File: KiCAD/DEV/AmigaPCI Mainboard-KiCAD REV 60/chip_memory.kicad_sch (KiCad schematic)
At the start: 25 parts, among them U701 74LVC245, U702 74LVC245, U703 74LVC245, U704 74LVC245, U705 74LVC245, U706 74LVC245, U707 SDRAM(8Mx32)

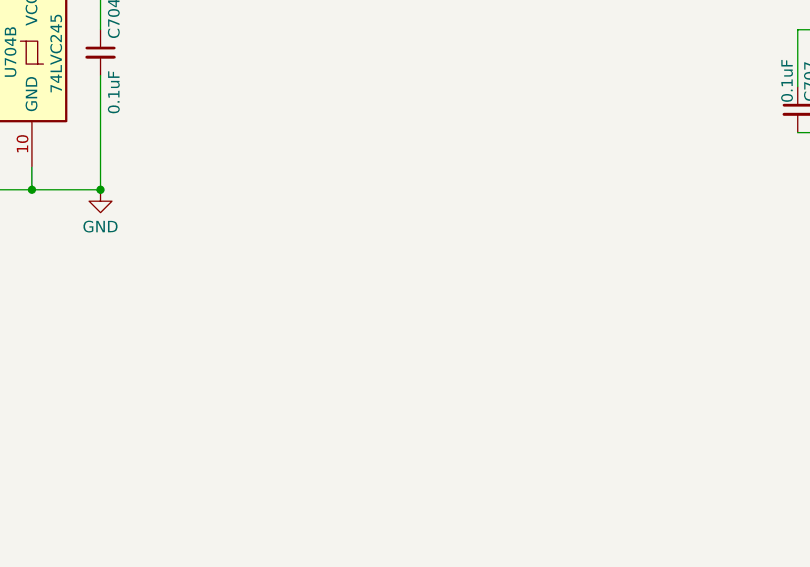
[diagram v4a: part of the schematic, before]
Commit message: Added SDRAM test points to APCI and Local Bus Card
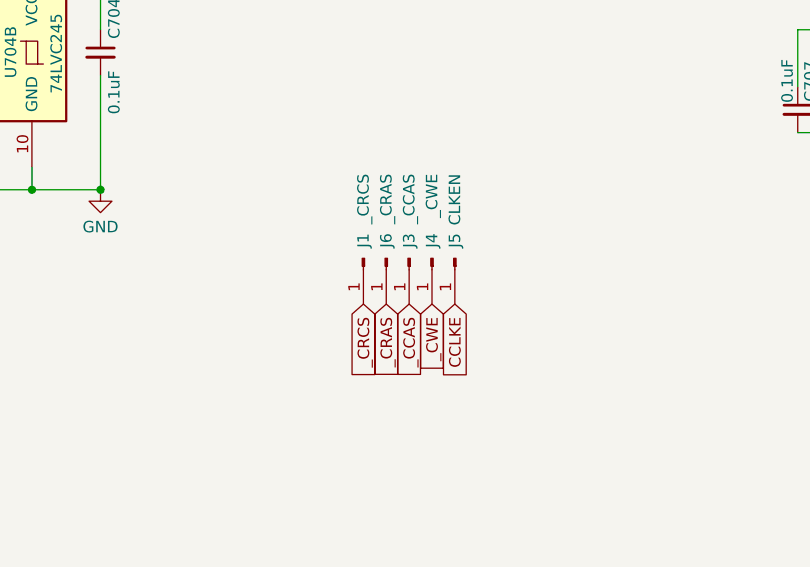
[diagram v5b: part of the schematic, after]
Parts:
- added J1: _CRCS, TestPoint:TestPoint_Pad_D1.0mm, symbol Connector:Conn_01x01_Pin
- added J3: _CCAS, TestPoint:TestPoint_Pad_D1.0mm, symbol Connector:Conn_01x01_Pin
- added J4: _CWE, TestPoint:TestPoint_Pad_D1.0mm, symbol Connector:Conn_01x01_Pin
- added J5: CLKEN, TestPoint:TestPoint_Pad_D1.0mm, symbol Connector:Conn_01x01_Pin
- added J6: _CRAS, TestPoint:TestPoint_Pad_D1.0mm, symbol Connector:Conn_01x01_Pin
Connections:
- net CCLKE: now also J5.1 (Pin_1)
- net _CCAS: now also J3.1 (Pin_1)
- net _CRAS: now also J6.1 (Pin_1)
- net _CRCS: now also J1.1 (Pin_1)
- net _CWE: now also J4.1 (Pin_1)
